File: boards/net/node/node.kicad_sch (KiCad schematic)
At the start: 60 parts, among them J1 N, J2 E, J3 S, J4 W, J5 SENSOR, J6 PROG, SW1 SW-18010P, U1 RP2040, U2 W25Q16JVSSIQ, U3 VL53L0CXV0DH/1, U4 ME6211C33M5G, Y1 12MHz

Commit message: net/node: pogo pads without paste apertures (Codex finding 4); pcbgen no_paste option
J6 now uses boards:PogoPads_2x04_P2.54mm (stock 2x4 SMD header minus F.Paste, no 3D model)
so DRC does not flag a library mismatch; the F.Paste gerber no longer contains J6.
pcbgen.footprint(no_paste=True) strips paste layers for the same purpose on stock
footprints (tested). make test, make check clean.

Co-Authored-By: Claude Fable 5.1 <noreply@anthropic.com>
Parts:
- J6: footprint Connector_PinHeader_2.54mm:PinHeader_2x04_P2.54mm_Vertical_SMD -> boards:PogoPads_2x04_P2.54mm
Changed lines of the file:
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@@
 			)
 		)
-		(property "Footprint" "Connector_PinHeader_2.54mm:PinHeader_2x04_P2.54mm_Vertical_SMD"
+		(property "Footprint" "boards:PogoPads_2x04_P2.54mm"
 			(at 370.84 55.88 90)
 			(effects

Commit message: net/node: LCSC numbers for every BOM line; crystal to ABM8-272-T3 with 15 pF
Every assembled line now has a verified JLCPCB part (make parts --boards
30: 0 errors, 0 warnings; 10 basic, 1 preferred, 9 extended). Passives
come from a PASSIVES table in schematic.py; descriptions carry the
real ratings.

- Y1: YXC X322512MSB4SI (C9002) is a 20 pF / 80 ohm part, not the 10 pF
  the design assumed. Switched to the RP2040 HDG crystal, Abracon
  ABM8-272-T3 (C20625731), with C1/C2 27 pF -> 15 pF C0G (C1644).
- D2/D4: WS2812B-2020 C965555 is discontinued; WS2812B-2020-V6
  (C52917434), same pinout.
- J1-J4: C144394 (3-pin B3B-XH-A; C144395 is the 4-pin B4B).
- J5 C32713273, U3 C91199, BZ1 C910763, D1 C81598, SW1 C2681585.

Regenerated node.kicad_sch/node.kicad_pcb: only fields, values and
descriptions differ (UUID-normalised); geometry, nets and fills are
unchanged. make check: 0 violations, 0 unconnected, 0 parity.

Co-Authored-By: Claude Opus 5.5 <noreply@anthropic.com>
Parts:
- BZ1: LCSC (none) -> C910763
- C1, C2: value 27p -> 15p; LCSC (none) -> C1644; MPN (none) -> CL10C150JB8NNNC; Manufacturer (none) -> Samsung
- C10, C14, C15, C16, C19, C20, C22, C3, C4, C5, C6, C7, C8, C9: LCSC (none) -> C14663; MPN (none) -> CC0603KRX7R9BB104; Manufacturer (none) -> Yageo
- C11, C13: LCSC (none) -> C15849; MPN (none) -> CL10A105KB8NNNC; Manufacturer (none) -> Samsung
- C12, C17, C18: LCSC (none) -> C96446; MPN (none) -> CL10A106MA8NRNC; Manufacturer (none) -> Samsung
- C21: LCSC (none) -> C19666; MPN (none) -> CL10A475KO8NNNC; Manufacturer (none) -> Samsung
- D1: LCSC (none) -> C81598; Manufacturer (none) -> Semtech
- D2, D4: value WS2812B-2020 -> WS2812B-2020-V6; LCSC (none) -> C52917434; MPN WS2812B-2020 -> WS2812B-2020-V6
- J1, J2, J3, J4: LCSC (none) -> C144394
- J5: LCSC (none) -> C32713273; MPN (none) -> HX PZ2.54-1x7P ZZ; Manufacturer (none) -> hanxia
- R1: LCSC (none) -> C21190; MPN (none) -> 0603WAF1001T5E; Manufacturer (none) -> UNI-ROYAL
- R10, R12, R14, R4, R5, R8: LCSC (none) -> C23162; MPN (none) -> 0603WAF4701T5E; Manufacturer (none) -> UNI-ROYAL
- R11, R13, R17, R18, R7, R9: LCSC (none) -> C22775; MPN (none) -> 0603WAF1000T5E; Manufacturer (none) -> UNI-ROYAL
- R15, R16: LCSC (none) -> C25190; MPN (none) -> 0603WAF270JT5E; Manufacturer (none) -> UNI-ROYAL
- R2, R3, R6: LCSC (none) -> C25804; MPN (none) -> 0603WAF1002T5E; Manufacturer (none) -> UNI-ROYAL
- SW1: LCSC (none) -> C2681585; Manufacturer (none) -> SHOU HAN
- U3: LCSC (none) -> C91199
- Y1: LCSC C9002 -> C20625731; MPN X322512MSB4SI -> ABM8-272-T3; Manufacturer YXC -> Abracon

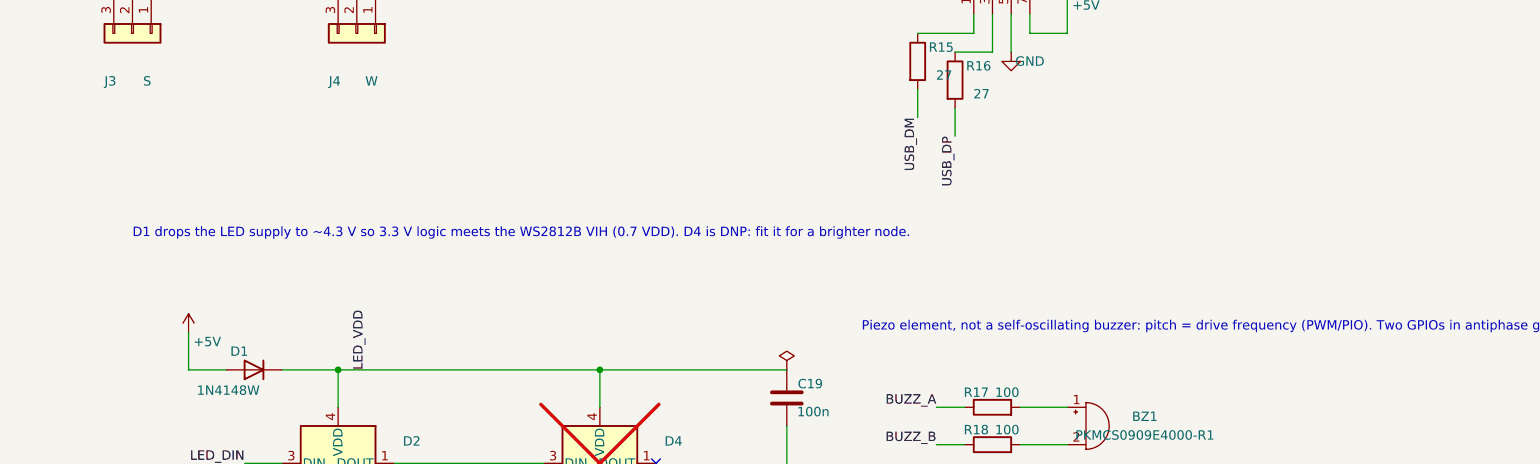
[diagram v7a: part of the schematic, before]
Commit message: net/node: side-entry JST S3B-XH-A link connectors, board re-placed
J1..J4 are now side-entry S3B-XH-A(LF)(SN) (C157928) on the middle of
each edge, mouths 1.1 mm past the edge, so cables leave in the board
plane and a node lies flat. Pinout per connector unchanged (1 = +5V,
2 = DATA, 3 = GND; straight cables); pin 1 is now the counter-clockwise
first pin on each edge. J4 sits 4.9 mm south of centre (U1's cap
column). Footprint: repo copy of the stock one with silk trimmed off
the board edge (pads, courtyard, fab and 3D identical).

J5, J6, BZ1, link resistors and some plane caps moved; the earlier
review fixes (C11, crystal loop, USB series R, pogo paste) are intact.
make check: 0 violations, 0 unconnected, 0 parity. LED note now quotes
the V6's VIH = 0.55 VDD. Order unpanelised (overhang).

Co-Authored-By: Claude Opus 5.5 <noreply@anthropic.com>
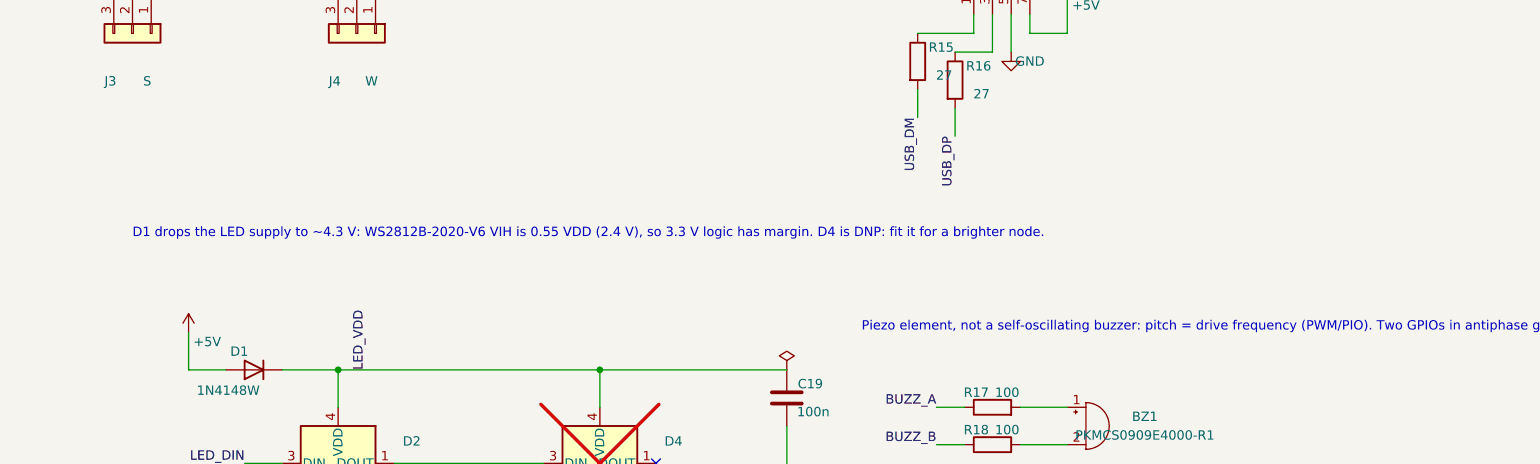
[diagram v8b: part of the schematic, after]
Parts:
- J1, J2, J3, J4: footprint Connector_JST:JST_XH_B3B-XH-A_1x03_P2.50mm_Vertical -> boards:JST_XH_S3B-XH-A_1x03_P2.50mm_Horizontal_EdgeMount; LCSC C144394 -> C157928; MPN B3B-XH-A(LF)(SN) -> S3B-XH-A(LF)(SN)
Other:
- note added: "D1 drops the LED supply to ~4.3 V: WS2812B-2020-V6 VIH is 0.55 VDD (2.4 V), so 3.3 V logic has margin. D4 is DNP: fit it for a brighter node."
- note removed: "D1 drops the LED supply to ~4.3 V so 3.3 V logic meets the WS2812B VIH (0.7 VDD). D4 is DNP: fit it for a brighter node."
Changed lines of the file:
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@@
 			)
 		)
-		(property "Footprint" "Connector_JST:JST_XH_B3B-XH-A_1x03_P2.50mm_Vertical"
+		(property "Footprint" "boards:JST_XH_S3B-XH-A_1x03_P2.50mm_Horizontal_EdgeMount"
 			(at 193.04 63.5 90)
 			(effects
@@
 			)
 		)
-		(property "Description" "JST XH 3-pin, vertical"
+		(property "Description" "JST XH 3-pin, side entry"
 			(at 193.04 63.5 90)
 			(effects
@@
 			)
 		)
-		(property "MPN" "B3B-XH-A(LF)(SN)"
+		(property "MPN" "S3B-XH-A(LF)(SN)"
 			(at 193.04 63.5 90)
 			(effects
@@
 			)
 		)
-		(property "LCSC" "C144394"
+		(property "LCSC" "C157928"
 			(at 193.04 63.5 90)
 			(effects
@@
 			)
 		)
-		(property "Footprint" "Connector_JST:JST_XH_B3B-XH-A_1x03_P2.50mm_Vertical"
+		(property "Footprint" "boards:JST_XH_S3B-XH-A_1x03_P2.50mm_Horizontal_EdgeMount"
 			(at 223.52 63.5 90)
 			(effects
@@
 			)
 		)
-		(property "Description" "JST XH 3-pin, vertical"
+		(property "Description" "JST XH 3-pin, side entry"
 			(at 223.52 63.5 90)
 			(effects
@@
 			)
 		)
-		(property "MPN" "B3B-XH-A(LF)(SN)"
+		(property "MPN" "S3B-XH-A(LF)(SN)"
 			(at 223.52 63.5 90)
 			(effects
@@
 			)
 		)
-		(property "LCSC" "C144394"
+		(property "LCSC" "C157928"
 			(at 223.52 63.5 90)
 			(effects
@@
 			)
 		)
-		(property "Footprint" "Connector_JST:JST_XH_B3B-XH-A_1x03_P2.50mm_Vertical"
+		(property "Footprint" "boards:JST_XH_S3B-XH-A_1x03_P2.50mm_Horizontal_EdgeMount"
 			(at 254 63.5 90)
 			(effects
@@
 			)
 		)
-		(property "Description" "JST XH 3-pin, vertical"
+		(property "Description" "JST XH 3-pin, side entry"
 			(at 254 63.5 90)
 			(effects
@@
 			)
 		)
-		(property "MPN" "B3B-XH-A(LF)(SN)"
+		(property "MPN" "S3B-XH-A(LF)(SN)"
 			(at 254 63.5 90)
 			(effects
@@
 			)
 		)
-		(property "LCSC" "C144394"
+		(property "LCSC" "C157928"
 			(at 254 63.5 90)
 			(effects
@@
 			)
 		)
-		(property "Footprint" "Connector_JST:JST_XH_B3B-XH-A_1x03_P2.50mm_Vertical"
+		(property "Footprint" "boards:JST_XH_S3B-XH-A_1x03_P2.50mm_Horizontal_EdgeMount"
 			(at 284.48 63.5 90)
 			(effects
@@
 			)
 		)
-		(property "Description" "JST XH 3-pin, vertical"
+		(property "Description" "JST XH 3-pin, side entry"
 			(at 284.48 63.5 90)
 			(effects
@@
 			)
 		)
-		(property "MPN" "B3B-XH-A(LF)(SN)"
+		(property "MPN" "S3B-XH-A(LF)(SN)"
 			(at 284.48 63.5 90)
 			(effects
@@
 			)
 		)
-		(property "LCSC" "C144394"
+		(property "LCSC" "C157928"
 			(at 284.48 63.5 90)
 			(effects
@@
 		)
 	)
-	(text "D1 drops the LED supply to ~4.3 V so 3.3 V logic meets the WS2812B VIH (0.7 VDD). D4 is DNP: fit it for a brighter node."
+	(text "D1 drops the LED supply to ~4.3 V: WS2812B-2020-V6 VIH is 0.55 VDD (2.4 V), so 3.3 V logic has margin. D4 is DNP: fit it for a brighter node."
 		(exclude_from_sim no)
 		(at 251.46 91.44 0)
